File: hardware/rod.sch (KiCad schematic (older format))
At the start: 11 parts, among them P1 CONN_01X12, P2 CONN_01X12, P3 GYRO, P4 DOTSTAR, SW1 SW_PUSH_R, SW2 SW_PUSH_G, SW3 SW_PUSH_B

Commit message: add current schematics and pcb
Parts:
- P1: footprint (none) -> Pin_Headers:Pin_Header_Straight_1x12_Pitch2.00mm
- P2: footprint (none) -> Pin_Headers:Pin_Header_Straight_1x12
- P3: footprint (none) -> Pin_Headers:Pin_Header_Straight_1x05
- P4: footprint (none) -> Pin_Headers:Pin_Header_Straight_1x04
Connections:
- net 10: now also P1.12 (P12)
- net 2: now also P2.5 (P5); no longer P2.2 (P2)
- net 4: now also P2.7 (P7); no longer P2.4 (P4)
- net 6: now also P2.9 (P9)
- net 7: now also P2.10 (P10)
- net A1: now also P1.7 (P7)
- net A2: now also P1.6 (P6)
- net GND: now also P1.2 (P2), P2.4 (P4)
- net PWR: now also P1.4 (P4)
- net e: now also P2.6 (P6); no longer P2.3 (P3)
- net TX: now reaches P2.1 (P1)
- net 8: now reaches P2.11 (P11)
- net 9: now reaches P2.12 (P12)
- net 5: now reaches P2.8 (P8)
- net 12: now reaches P1.10 (P10)
- net 11: now reaches P1.11 (P11)
- net A0: now reaches P1.8 (P8)
- net 13: now reaches P1.9 (P9)
- new net RX: P2.2 (P2)
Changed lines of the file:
@@
 F 0 "P2" H 2550 2750 50  0000 C CNN
 F 1 "CONN_01X12" V 2650 2100 50  0000 C CNN
-F 2 "" H 2550 2100 50  0001 C CNN
+F 2 "Pin_Headers:Pin_Header_Straight_1x12" H 2550 2100 50  0001 C CNN
 F 3 "" H 2550 2100 50  0000 C CNN
 	1    2550 2100
@@
 F 0 "P1" H 2550 2200 50  0000 C CNN
 F 1 "CONN_01X12" V 2650 1550 50  0000 C CNN
-F 2 "" H 2550 1550 50  0001 C CNN
+F 2 "Pin_Headers:Pin_Header_Straight_1x12_Pitch2.00mm" H 2550 1550 50  0001 C CNN
 F 3 "" H 2550 1550 50  0000 C CNN
 	1    2550 1550
@@
 F 0 "P3" H 3700 1700 50  0000 C CNN
 F 1 "GYRO" V 3800 1400 50  0000 C CNN
-F 2 "" H 3700 1400 50  0001 C CNN
+F 2 "Pin_Headers:Pin_Header_Straight_1x05" H 3700 1400 50  0001 C CNN
 F 3 "" H 3700 1400 50  0000 C CNN
 	1    3700 1400
@@
 F 0 "P4" H 4450 1650 50  0000 C CNN
 F 1 "DOTSTAR" V 4550 1400 50  0000 C CNN
-F 2 "" H 4450 1400 50  0001 C CNN
+F 2 "Pin_Headers:Pin_Header_Straight_1x04" H 4450 1400 50  0001 C CNN
 F 3 "" H 4450 1400 50  0000 C CNN
 	1    4450 1400
@@
 Text GLabel 4950 1450 3    60   Input ~ 0
 10
+Text GLabel 2400 2300 3    60   Input ~ 0
+2
+Text GLabel 2500 2300 3    60   Input ~ 0
+e
+Text GLabel 2600 2300 3    60   Input ~ 0
+4
+Text GLabel 3100 1350 1    60   Input ~ 0
+10
+Text GLabel 3000 1350 1    60   Input ~ 0
+11
+Text GLabel 2900 1350 1    60   Input ~ 0
+12
+Text GLabel 2800 1350 1    60   Input ~ 0
+13
+Text GLabel 2700 1350 1    60   Input ~ 0
+A0
+Text GLabel 2600 1350 1    60   Input ~ 0
+A1
+Text GLabel 2500 1350 1    60   Input ~ 0
+A2
+Text GLabel 2100 1350 1    60   Input ~ 0
+GND
+Text GLabel 2300 1350 1    60   Input ~ 0
+PWR
+Text GLabel 2000 2300 3    60   Input ~ 0
+TX
 Text GLabel 2100 2300 3    60   Input ~ 0
-2
-Text GLabel 2200 2300 3    60   Input ~ 0
-e
+RX
 Text GLabel 2300 2300 3    60   Input ~ 0
-4
+GND
+Text GLabel 2700 2300 3    60   Input ~ 0
+5
+Text GLabel 2800 2300 3    60   Input ~ 0
+6
+Text GLabel 2900 2300 3    60   Input ~ 0
+7
+Text GLabel 3000 2300 3    60   Input ~ 0
+8
+Text GLabel 3100 2300 3    60   Input ~ 0
+9
 $EndSCHEMATC

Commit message: Updated PCB
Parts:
- added P5: USB_B, Connect:USB_B, symbol USB_B
- P1: value CONN_01X12 -> arduino_mini; footprint Pin_Headers:Pin_Header_Straight_1x12_Pitch2.00mm -> Pin_Headers:Pin_Header_Straight_1x12
- P2: value CONN_01X12 -> arduino_mini
- SW2: value SW_PUSH_G -> SW_PUSH_B
- SW3: value SW_PUSH_B -> SW_PUSH_G
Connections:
- net e is gone; now on net 3: P2.6 (P6)
- net 10: no longer BZ1.1
- net 2: now also P4.3 (P3); no longer R3.2, SW3.2
- net 3: now also P4.2 (P2); no longer R2.2, SW2.2
- net 4: now also R3.2, SW3.2; no longer R1.2, SW1.2
- net 5: now also R2.2, SW2.2
- net 6: now also R1.2, SW1.2; no longer P4.2 (P2)
- net 7: now also BZ1.1; no longer P4.3 (P3)
- net A3: now also P1.5 (P5)
- net GND: now also P5.4 (GND); no longer P2.4 (P4)
- net PWR: now also P5.1 (VCC)
- net RX: now also P5.3 (D+)
- net TX: now also P5.2 (D-)
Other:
- moved on the sheet: BZ1, P1, P2, P3, P4, R1, R2, R3, SW1, SW2, SW3

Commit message: Signed-off-by: Edith Li <abenoy05@gmail.com>
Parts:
- P1, P2: value arduino_mini -> CONN_01X12
- R1, R2, R3: footprint Resistors_ThroughHole:Resistor_Horizontal_RM10mm -> Resistors_SMD:R_1206
- SW2: value SW_PUSH_B -> SW_PUSH_G
- SW3: value SW_PUSH_G -> SW_PUSH_B
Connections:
- net GND: now also P2.4 (P4)
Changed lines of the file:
@@
 P 4650 2400
 F 0 "P2" H 4650 3050 50  0000 C CNN
-F 1 "arduino_mini" V 4750 2400 50  0000 C CNN
+F 1 "CONN_01X12" V 4750 2400 50  0000 C CNN
 F 2 "Pin_Headers:Pin_Header_Straight_1x12" H 4650 2400 50  0001 C CNN
 F 3 "" H 4650 2400 50  0000 C CNN
@@
 P 5200 2400
 F 0 "P1" H 5200 3050 50  0000 C CNN
-F 1 "arduino_mini" V 5300 2400 50  0000 C CNN
+F 1 "CONN_01X12" V 5300 2400 50  0000 C CNN
 F 2 "Pin_Headers:Pin_Header_Straight_1x12" H 5200 2400 50  0001 C CNN
 F 3 "" H 5200 2400 50  0000 C CNN
@@
 F 0 "R1" V 4480 3900 50  0000 C CNN
 F 1 "R" V 4400 3900 50  0000 C CNN
-F 2 "Resistors_ThroughHole:Resistor_Horizontal_RM10mm" V 4330 3900 50  0001 C CNN
+F 2 "Resistors_SMD:R_1206" V 4330 3900 50  0001 C CNN
 F 3 "" H 4400 3900 50  0000 C CNN
 	1    4400 3900
@@
 F 0 "R2" V 4480 5050 50  0000 C CNN
 F 1 "R" V 4400 5050 50  0000 C CNN
-F 2 "Resistors_ThroughHole:Resistor_Horizontal_RM10mm" V 4330 5050 50  0001 C CNN
+F 2 "Resistors_SMD:R_1206" V 4330 5050 50  0001 C CNN
 F 3 "" H 4400 5050 50  0000 C CNN
 	1    4400 5050
@@
 P 4650 4750
 F 0 "SW2" H 4800 4860 50  0000 C CNN
-F 1 "SW_PUSH_B" H 4650 4670 50  0000 C CNN
+F 1 "SW_PUSH_G" H 4650 4670 50  0000 C CNN
 F 2 "Buttons_Switches_ThroughHole:SW_PUSH-12mm" H 4650 4750 50  0001 C CNN
 F 3 "" H 4650 4750 50  0000 C CNN
@@
 F 0 "R3" V 4480 6200 50  0000 C CNN
 F 1 "R" V 4400 6200 50  0000 C CNN
-F 2 "Resistors_ThroughHole:Resistor_Horizontal_RM10mm" V 4330 6200 50  0001 C CNN
+F 2 "Resistors_SMD:R_1206" V 4330 6200 50  0001 C CNN
 F 3 "" H 4400 6200 50  0000 C CNN
 	1    4400 6200
@@
 P 4650 5900
 F 0 "SW3" H 4800 6010 50  0000 C CNN
-F 1 "SW_PUSH_G" H 4650 5820 50  0000 C CNN
+F 1 "SW_PUSH_B" H 4650 5820 50  0000 C CNN
 F 2 "Buttons_Switches_ThroughHole:SW_PUSH-12mm" H 4650 5900 50  0001 C CNN
 F 3 "" H 4650 5900 50  0000 C CNN
@@
 Text GLabel 5400 2150 2    60   Input ~ 0
 PWR
+Text GLabel 4450 1850 0    60   Input ~ 0
+TX
+Text GLabel 4450 1950 0    60   Input ~ 0
+RX
+Text GLabel 4450 2150 0    60   Input ~ 0
+GND
 Text GLabel 4450 2550 0    60   Input ~ 0
 5
@@
 Text GLabel 4450 2950 0    60   Input ~ 0
 9
+$Comp
+L USB_B P5
+U 1 1 5849FBDE
+P 5050 6850
+F 0 "P5" H 5250 6650 50  0000 C CNN
+F 1 "USB_B" H 5000 7050 50  0000 C CNN
+F 2 "Connect:USB_B" V 5000 6750 50  0001 C CNN
+F 3 "" V 5000 6750 50  0000 C CNN
+	1    5050 6850
+	1    0    0    -1
+$EndComp
+Text GLabel 4850 7150 3    60   Input ~ 0
+PWR
+Text GLabel 5150 7150 3    60   Input ~ 0
+GND
+Text GLabel 4950 7150 3    60   Input ~ 0
+TX
+Text GLabel 5050 7150 3    60   Input ~ 0
+RX
 Text GLabel 5400 2250 2    60   Input ~ 0
 A3
-$Comp
-L USB_B P5
-U 1 1 5849C52D
-P 4750 6850
-F 0 "P5" H 4950 6650 50  0000 C CNN
-F 1 "USB_B" H 4700 7050 50  0000 C CNN
-F 2 "Connect:USB_B" V 4700 6750 50  0001 C CNN
-F 3 "" V 4700 6750 50  0000 C CNN
-	1    4750 6850
-	1    0    0    -1
-$EndComp
-Text GLabel 4450 1850 0    60   Input ~ 0
-TX
-Text GLabel 4450 1950 0    60   Input ~ 0
-RX
-Text GLabel 4650 7150 3    60   Input ~ 0
-TX
-Text GLabel 4750 7150 3    60   Input ~ 0
-RX
-Text GLabel 4850 7150 3    60   Input ~ 0
-GND
-Text GLabel 4550 7150 3    60   Input ~ 0
-PWR
 $EndSCHEMATC

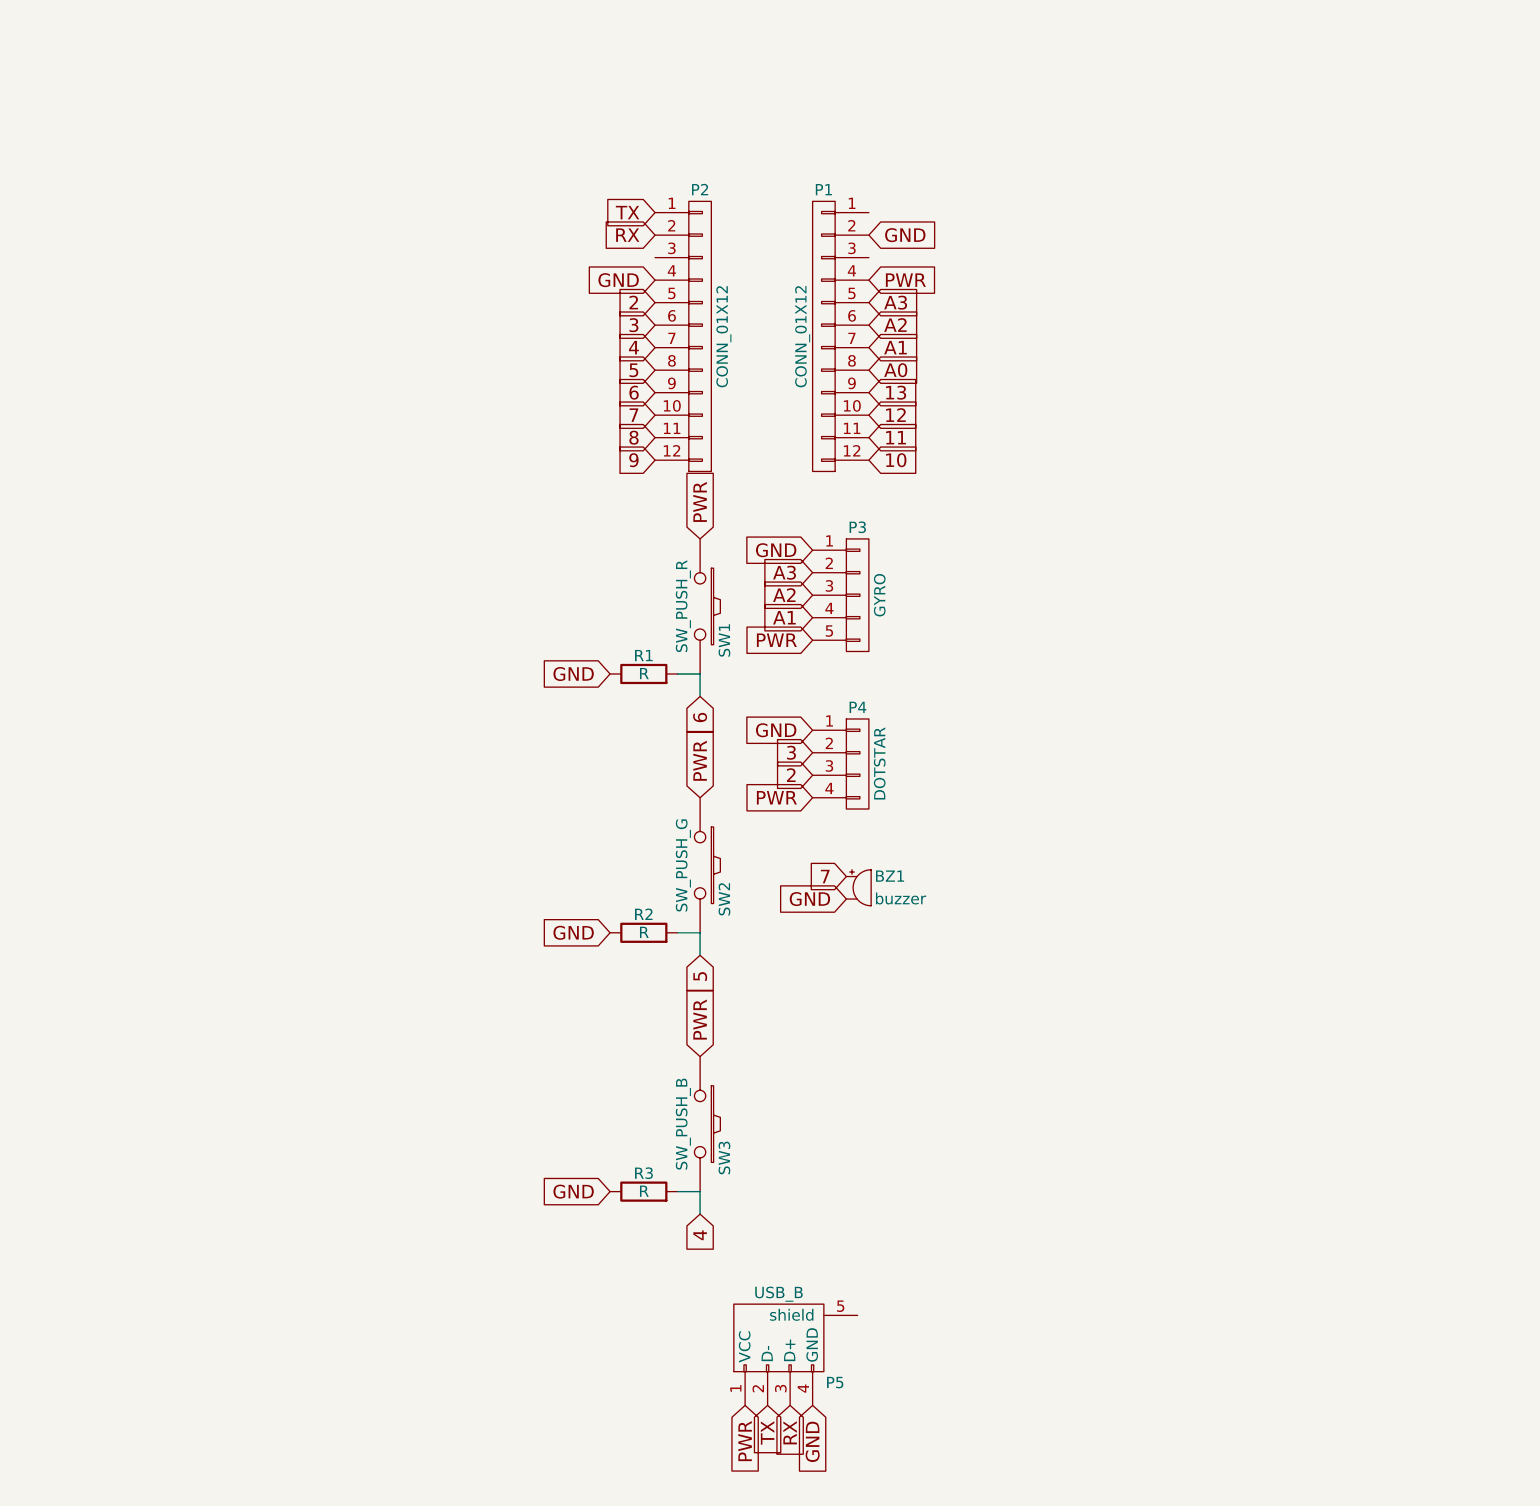
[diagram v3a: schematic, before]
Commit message: updated semi-final version of rod pcb schematics and layout
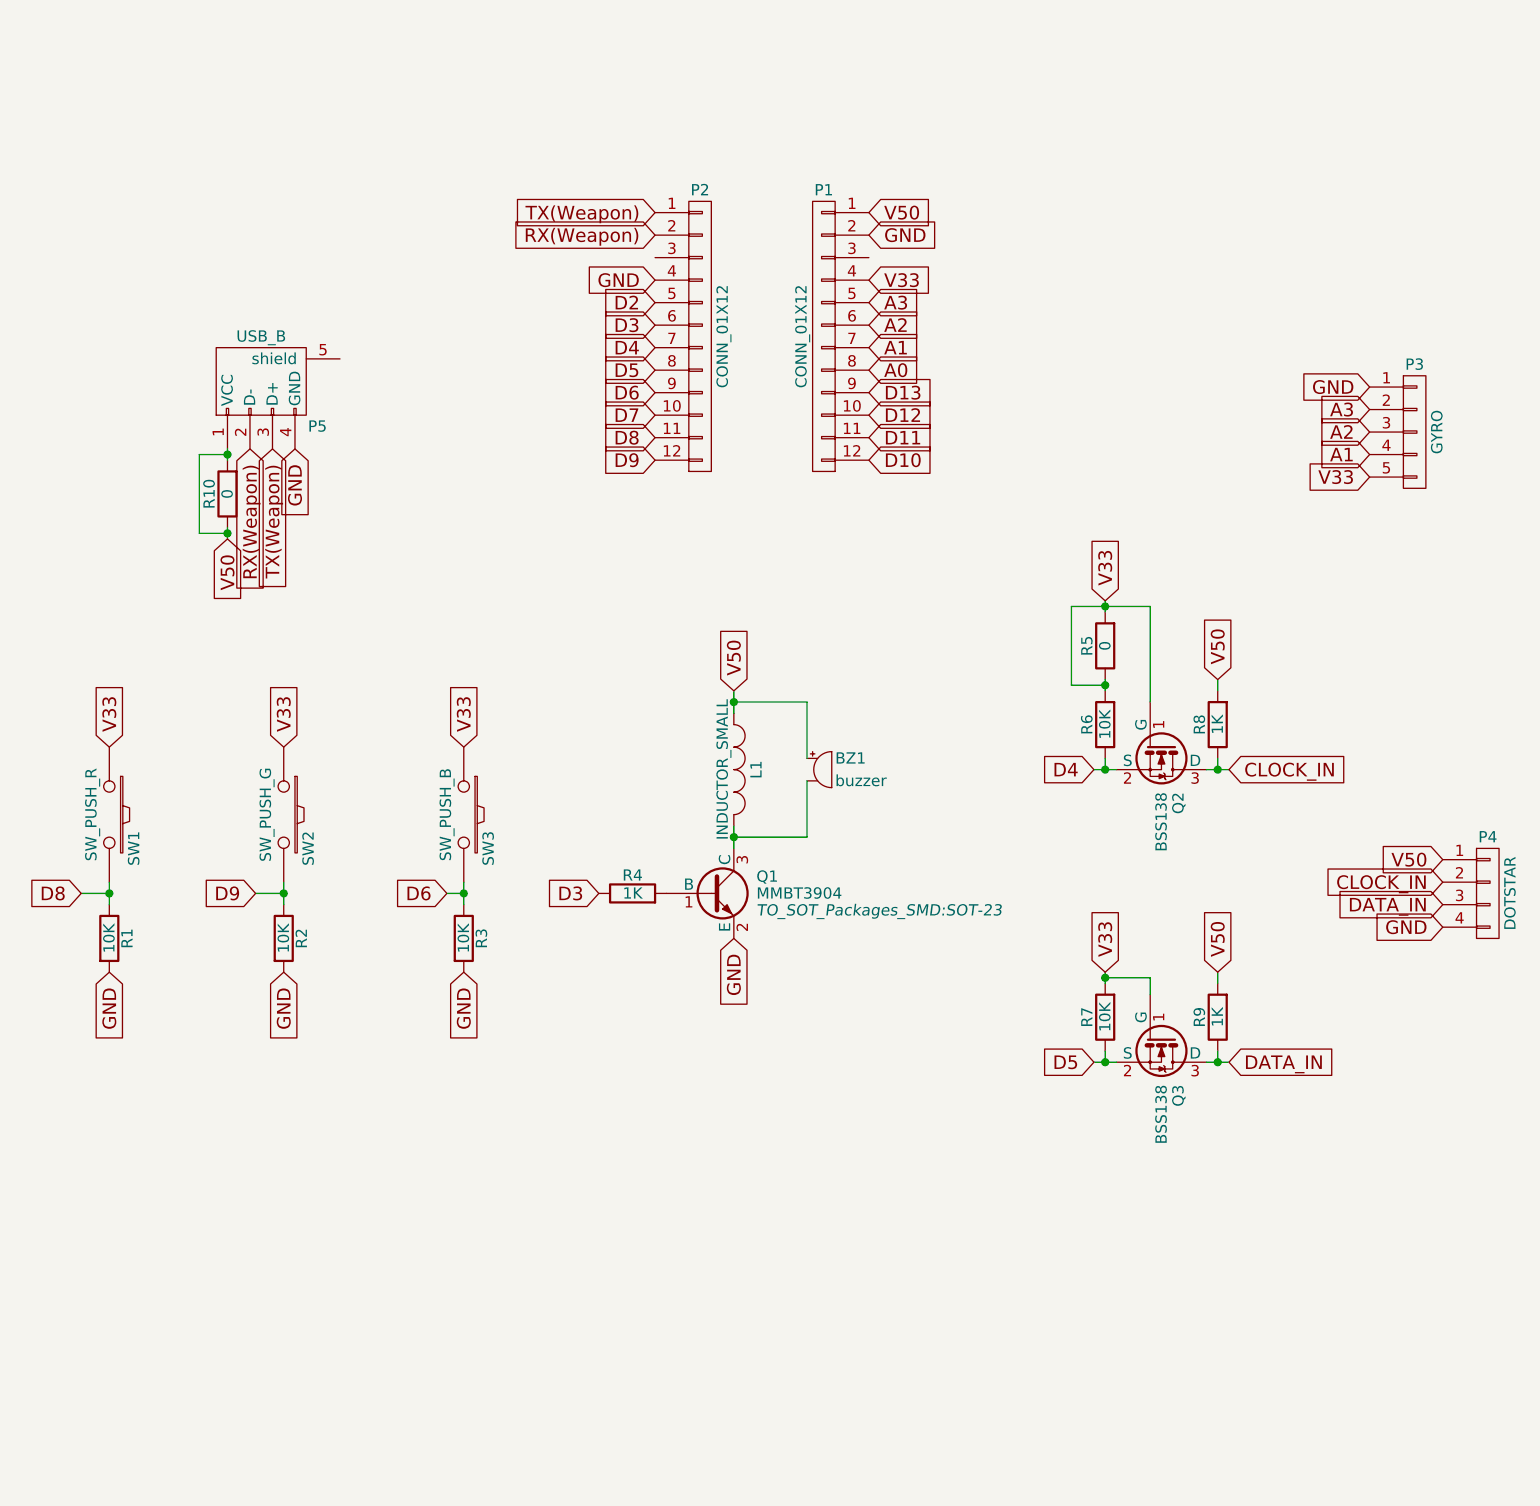
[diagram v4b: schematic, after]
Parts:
- added L1: INDUCTOR_SMALL, Resistors_Universal:Resistor_SMD+THTuniversal_1206_RM10_HandSoldering, symbol INDUCTOR_SMALL
- added Q1: MMBT3904, TO_SOT_Packages_SMD:SOT-23, symbol MMBT3904
- added Q2, Q3: BSS138, TO_SOT_Packages_SMD:SOT-23, symbol BSS138
- added R10: 0, Resistors_Universal:Resistor_SMD+THTuniversal_2512_RM10_HandSoldering, symbol R
- added R4, R8, R9: 1K, Resistors_SMD:R_1206, symbol R
- added R5: 0, Resistors_SMD:R_1206, symbol R
- added R6, R7: 10K, Resistors_SMD:R_1206, symbol R
- BZ1: footprint Buzzers_Beepers:MagneticBuzzer_Kingstate_KCG0601 -> Buzzers_Beepers:Buzzer_12x9.5RM7.6
- R1, R2, R3: value R -> 10K
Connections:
- net GND: now also P4.4 (P4), R1.2, R2.2, R3.2, Q1.2 (E); no longer BZ1.2, P4.1 (P1), R1.1, R2.1, R3.1
- net V50: now reaches P1.1 (P1)
- net V50: now also BZ1.1, P4.1 (P1), P5.1 (VCC), L1.1, R10.1, R10.2, R8.2, R9.2
- net 10 renamed D10
- net 11 renamed D11
- net 12 renamed D12
- net 13 renamed D13
- net 2 renamed D2
- net D2: no longer P4.3 (P3)
- net 3 renamed CLOCK_IN
- net CLOCK_IN: now also Q2.3 (D), R8.1; no longer P2.6 (P6)
- removed net 4: P2.7 (P7), R3.2, SW3.2
- removed net 5: P2.8 (P8), R2.2, SW2.2
- removed net 6: P2.9 (P9), R1.2, SW1.2
- net 7 renamed D7
- net D7: no longer BZ1.1
- net 8 renamed D8
- net D8: now also R1.1, SW1.2
- net 9 renamed D9
- net D9: now also R2.1, SW2.2
- net PWR renamed V33
- net V33: now also Q2.1 (G), Q3.1 (G), R5.1, R5.2, R6.2, R7.2; no longer P4.4 (P4), P5.1 (VCC)
- net RX renamed RX(Weapon)
- net RX(Weapon): now also P5.2 (D-); no longer P5.3 (D+)
- net TX renamed TX(Weapon)
- net TX(Weapon): now also P5.3 (D+); no longer P5.2 (D-)
- new net: BZ1.2, L1.2, Q1.3 (C)
- new net: Q1.1 (B), R4.2
- new net D3: P2.6 (P6), R4.1
- new net D4: P2.7 (P7), Q2.2 (S), R6.1
- new net D5: P2.8 (P8), Q3.2 (S), R7.1
- new net D6: P2.9 (P9), R3.1, SW3.2
- new net DATA_IN: P4.3 (P3), Q3.3 (D), R9.1
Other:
- moved on the sheet: BZ1, P3, P4, P5, R1, R2, R3, SW1, SW2, SW3
